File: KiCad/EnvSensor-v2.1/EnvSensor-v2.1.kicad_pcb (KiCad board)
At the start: 2 copper layers, 100 x 100 mm, 90 parts, among them J1 BattSense, J2 USB_B_Micro, J3 USB_C_Plug_USB2.0, J4 USB_C_Receptacle_USB2.0, J5 Conn_01x02, J6 Conn_01x02, Q1 AO6804A, Q2 IRLML2502, Q3 ZXMP6A16K, SW1 BATT_SWITCH, SW2 Start, U1 AP9101CK, U2 MCP1826S-5.0, U3 LM2735XMF, U4 MCP73843-4.2, U5 MCP1825S-3.3, U6 LTC3440

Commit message: pcb started
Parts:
- removed the J3 at (152.6, 105.2)
- added C13: 2u2, Capacitor_SMD:C_1206_3216Metric, F.Cu at (226.0, 162.0)
- added C14: 2u2, Capacitor_SMD:C_1206_3216Metric, F.Cu at (233.0, 163.0)
- added C16: 2u2, Capacitor_SMD:C_1206_3216Metric, F.Cu at (132.0, 144.0)
- added C17: 2u2, Capacitor_SMD:C_1206_3216Metric, F.Cu at (139.0, 144.0)
- added C19: 22u, Capacitor_SMD:C_1206_3216Metric, F.Cu at (133.0, 180.0)
- added C2: 4n7, Capacitor_SMD:C_0805_2012Metric, F.Cu at (193.2, 52.8)
- added C20: 22u, Capacitor_SMD:C_1206_3216Metric, F.Cu at (133.0, 186.0)
- added C21: 47u, Capacitor_SMD:C_1206_3216Metric, F.Cu at (162.0, 177.0)
- added C22: 47u, Capacitor_SMD:C_1206_3216Metric, F.Cu at (161.0, 182.0)
- added C26: 1u, Capacitor_SMD:C_0805_2012Metric, F.Cu at (66.0, 136.0)
- added C27: 47n, Capacitor_SMD:C_0805_2012Metric, F.Cu at (87.0, 165.0)
- added C33: 2u2, Capacitor_SMD:C_1206_3216Metric, F.Cu at (251.0, 94.0)
- added C35: 2u2, Capacitor_SMD:C_1206_3216Metric, F.Cu at (258.0, 94.0)
- added C36: 22n, Capacitor_SMD:C_0805_2012Metric, F.Cu at (83.0, 168.0)
- added C40: 2u2, Capacitor_SMD:C_1206_3216Metric, F.Cu at (191.0, 104.0)
- added C41: 2u2, Capacitor_SMD:C_1206_3216Metric, F.Cu at (197.0, 104.0)
- added C42: 100n, Capacitor_SMD:C_0603_1608Metric, F.Cu at (73.0, 169.0)
- added D1: PESD5V0V1BA, Diode_SMD:D_SOD-323, F.Cu at (108.0, 51.0)
- added D10: INPUT POWER LED, LED_THT:LED_D3.0mm_Horizontal_O3.81mm_Z6.0mm, F.Cu at (72.0, 141.0)
- added D11: POWER LED, LED_SMD:LED_0805_2012Metric, F.Cu at (83.0, 130.0)
- added D12: CHARGE LED, LED_THT:LED_D3.0mm_Horizontal_O3.81mm_Z6.0mm, F.Cu at (83.0, 135.0)
- added D13: 3.3V POWER LED, LED_THT:LED_D3.0mm_Horizontal_O3.81mm_Z6.0mm, F.Cu at (154.2, 49.8)
- added D14: 5V POWER LED, LED_THT:LED_D3.0mm_Horizontal_O3.81mm_Z6.0mm, F.Cu at (166.3, 49.8)
- added D9: POWER LED, LED_SMD:LED_0805_2012Metric, F.Cu at (73.0, 134.0)
- added J6: POWER_OUTPUT, Connector_PinHeader_2.54mm:PinHeader_2x07_P2.54mm_Vertical, F.Cu at (117.3, 90.6)
- added JP5: NC, Jumper:SolderJumper-2_P1.3mm_Bridged_RoundedPad1.0x1.5mm, F.Cu at (143.0, 172.0)
- added JP6: NO, Jumper:SolderJumper-2_P1.3mm_Open_RoundedPad1.0x1.5mm, F.Cu at (143.0, 176.0)
- added L2: 100-600, Inductor_SMD:L_0805_2012Metric, F.Cu at (228.0, 156.0)
- added L3: 100-600R, Inductor_SMD:L_0805_2012Metric, F.Cu at (137.0, 139.0)
- added L4: 1u, Inductor_SMD:L_TDK_SLF10145, F.Cu at (146.0, 192.0)
- added L6: 100-600R, Inductor_SMD:L_0805_2012Metric, F.Cu at (253.0, 89.0)
- added L7: 100-600R, Inductor_SMD:L_0805_2012Metric, F.Cu at (194.0, 101.0)
- added R16: 73k2, Resistor_SMD:R_0805_2012Metric, F.Cu at (155.0, 176.0)
- added R17: 120k, Resistor_SMD:R_0805_2012Metric, F.Cu at (155.0, 181.0)
- added R18: 3k3, Resistor_SMD:R_0805_2012Metric, F.Cu at (34.0, 141.0)
- added R2: 5k1, Resistor_SMD:R_0805_2012Metric, F.Cu at (108.0, 49.0)
- added R20: 30k, Resistor_SMD:R_0805_2012Metric, F.Cu at (155.0, 186.0)
- added R23: 4R7, Resistor_SMD:R_0805_2012Metric, F.Cu at (66.0, 130.0)
- added R24: DNP, Resistor_SMD:R_1206_3216Metric, F.Cu at (69.0, 158.0)
- added R25: 0R05, Resistor_SMD:R_1206_3216Metric, F.Cu at (69.0, 163.0)
- added R26: 10k, Resistor_SMD:R_0603_1608Metric, F.Cu at (78.0, 163.0)
- added R27: 3k3, Resistor_SMD:R_0805_2012Metric, F.Cu at (68.0, 145.0)
- added R28: 3k3, Resistor_SMD:R_0805_2012Metric, F.Cu at (85.0, 124.0)
- added R29: 3k3, Resistor_SMD:R_0805_2012Metric, F.Cu at (180.6, 67.4)
- added R30: 3k3, Resistor_SMD:R_0805_2012Metric, F.Cu at (176.1, 72.2)
- added R4: 50R, Resistor_SMD:R_2512_6332Metric, F.Cu at (161.8, 67.1)
- added R6: 12R5, Resistor_SMD:R_2512_6332Metric, F.Cu at (156.8, 62.2)
- added TP1: TestPoint, TestPoint:TestPoint_Pad_D1.5mm, F.Cu at (201.6, 53.3)
- added TP2: TestPoint, TestPoint:TestPoint_Pad_D1.5mm, F.Cu at (197.9, 56.0)
- added TP3: TestPoint, TestPoint:TestPoint_Pad_D1.5mm, F.Cu at (193.3, 62.6)
- added TP4: TestPoint, TestPoint:TestPoint_Pad_D1.5mm, F.Cu at (174.2, 80.3)
- added TP5: TestPoint, TestPoint:TestPoint_Pad_D1.5mm, F.Cu at (184.6, 70.7)
- added TP6: TestPoint, TestPoint:TestPoint_Pad_D1.5mm, F.Cu at (180.1, 73.6)
- added U4: TPS631000, Package_TO_SOT_SMD:SOT-23-8, F.Cu at (148.0, 179.0)
- added U7: LTC4052, Package_SO:MSOP-8_3x3mm_P0.65mm, F.Cu at (83.0, 155.0)
- C1: value 10n -> 4n7
- D2: renamed from D7; value PMEG2010AEJ -> DNP (PMEG2010AEJ)
- D3: renamed from D8; value PMEG3020BER -> DNP (PMEG3020BER)
- Q2: value IRLML2502 -> IRLML2244
- R1: value 3k -> 5k1
- R3: value 10k -> 100R; footprint Resistor_SMD:R_0603_1608Metric -> Resistor_SMD:R_2512_6332Metric
- R5: value 100k -> 25R; footprint Resistor_SMD:R_0603_1608Metric -> Resistor_SMD:R_2512_6332Metric
- TS1: renamed from TS4; footprint TestPoint:TestPoint_THTPad_D1.5mm_Drill0.7mm -> TestPoint:TestPoint_Pad_D1.5mm
- TS2: renamed from TS5; footprint TestPoint:TestPoint_THTPad_D1.5mm_Drill0.7mm -> TestPoint:TestPoint_Pad_D1.5mm
- TS3: renamed from TS6; footprint TestPoint:TestPoint_THTPad_D1.5mm_Drill0.7mm -> TestPoint:TestPoint_Pad_D1.5mm
- TS4: renamed from TS7; footprint TestPoint:TestPoint_THTPad_D1.5mm_Drill0.7mm -> TestPoint:TestPoint_Pad_D1.5mm
- TS5: renamed from TS1; footprint TestPoint:TestPoint_THTPad_D1.5mm_Drill0.7mm -> TestPoint:TestPoint_Pad_D1.5mm
- TS6: renamed from TS2; footprint TestPoint:TestPoint_THTPad_D1.5mm_Drill0.7mm -> TestPoint:TestPoint_Pad_D1.5mm
- TS7: renamed from TS3; footprint TestPoint:TestPoint_THTPad_D1.5mm_Drill0.7mm -> TestPoint:TestPoint_Pad_D1.5mm
- moved D7 259.7 mm to (40.0, 157.0)
- moved R21 258.4 mm to (33.0, 163.0)
- moved C23 235.1 mm to (49.0, 135.0)
- moved D5 234.3 mm to (23.0, 138.0)
- moved H1 217.8 mm to (26.0, 24.0)
- moved D6 214.9 mm to (22.0, 131.0)
- moved C24 208.9 mm to (49.0, 154.0)
- moved C18 208.6 mm to (30.0, 136.0)
- moved H4 204.3 mm to (23.0, 116.0)
- moved Q2 203.9 mm to (34.0, 132.0)
- moved C25 186.7 mm to (50.0, 161.0)
- moved R19 174.7 mm to (23.0, 145.0)
- moved R1 156.3 mm to (108.0, 47.0), turned to 180 degrees
- moved U5 132.0 mm to (26.0, 156.0)
- moved R22 128.6 mm to (33.0, 148.0)
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- renumbered C23 to C10, C24 to C11, C25 to C12, C20 to C15, C3 to C18, C4 to C23, C14 to C24, C15 to C25, C5 to C28, C6 to C29, C16 to C3, C7 to C30, C8 to C31, C9 to C32, C10 to C34, C11 to C37, C12 to C38, C13 to C39, C17 to C4, C18 to C5, C19 to C6, C2 to C7, C21 to C8, C22 to C9, D2 to D15, D1 to D4, D3 to D5, D4 to D6, D5 to D7, D6 to D8, J2 to J1, J4 to J2, J1 to J3, J6 to J4, JP4 to JP2, JP5 to JP3, JP3 to JP4, JP2 to JP7, L2 to L1, L1 to L5, R15 to R10, R16 to R11, R17 to R12, R18 to R13, R19 to R14, R6 to R15, R8 to R19, R11 to R21, R12 to R22, R7 to R31, R9 to R32, R10 to R33, R13 to R34, R2 to R7, R14 to R8, R4 to R9, U6 to U1, U1 to U2, U5 to U3, U4 to U5, U2 to U6, U3 to U8
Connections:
- net Net-(C20-Pad1) renamed /3V3_REG
- net Net-(D8-Pad2) renamed /3V3_LTC_SW2
- net Net-(R14-Pad2) renamed /3V3_LTC_FB
- C1 pad 1: BATTERY_MEASURE_INPUT -> Net-(C1-Pad1)
- C10 pad 1: +BATT -> /BATT_3V3_FILTER
- C18 pad 1: Net-(C3-Pad1) -> Net-(C18-Pad1)
- C28 pad 1: Net-(C5-Pad1) -> Net-(C28-Pad1)
- C29 pad 1: Net-(C5-Pad1) -> Net-(C28-Pad1)
- C3 pad 1: Net-(C16-Pad1) -> /3V3_NOT_REG
- C30 pad 1: Net-(C5-Pad1) -> Net-(C28-Pad1)
- C31 pad 1: Net-(C5-Pad1) -> Net-(C28-Pad1)
- C32 pad 1: Net-(C5-Pad1) -> Net-(C28-Pad1)
- C37 pad 1: +BATT -> Net-(C37-Pad1)
- C38 pad 1: +BATT -> Net-(C37-Pad1)
- C39 pad 1: +BATT -> Net-(C37-Pad1)
- C4 pad 1: Net-(C16-Pad1) -> /3V3_NOT_REG
- C5 pad 1: Net-(C16-Pad1) -> /3V3_NOT_REG
- C6 pad 1: Net-(C16-Pad1) -> /3V3_NOT_REG
- C8 pad 1: +BATT -> /BATT_3V3_FILTER
- C9 pad 1: +BATT -> /BATT_3V3_FILTER
- D15 pad 1: Net-(C5-Pad1) -> Net-(C28-Pad1)
- D2 pad 1: Net-(D7-Pad1) (its old number) -> /3V3_LTC_SW1
- D3 pad 1: Net-(C16-Pad1) -> /3V3_NOT_REG
- D4 pad 1: Net-(C3-Pad1) -> unconnected-(D4-Pad1)
- D4 pad 2: VBUS -> unconnected-(D4-Pad2)
- D7 pad 2: Net-(C3-Pad1) -> Net-(C18-Pad1)
- D8 pad 2: Net-(C3-Pad1) -> Net-(C18-Pad1)
- J1 pad 6: unconnected-(J2-Pad6) -> Net-(C1-Pad1)
- J2 pad A1: Net-(J4-PadA1) -> GND
- J2 pad A12: Net-(J4-PadA1) -> GND
- J2 pad A4: Net-(J4-PadA4) -> VBUS
- J2 pad A5: unconnected-(J4-PadA5) -> Net-(J2-PadA5)
- J2 pad A9: Net-(J4-PadA4) -> VBUS
- J2 pad B1: Net-(J4-PadA1) -> GND
- J2 pad B12: Net-(J4-PadA1) -> GND
- J2 pad B4: Net-(J4-PadA4) -> VBUS
- J2 pad B5: unconnected-(J4-PadB5) -> Net-(J2-PadB5)
- J2 pad B9: Net-(J4-PadA4) -> VBUS
- J2 pad S1: unconnected-(J4-PadS1) -> Net-(C2-Pad1)
- JP2 pad 1: +BATT -> /BATT_3V3_FILTER
- L1 pad 1: Net-(D7-Pad1) (its old number) -> /3V3_LTC_SW1
- L5 pad 1: +BATT -> Net-(C37-Pad1)
- Q2 pad 1: BATTERY_MEASURE_ENABLE -> Net-(Q2-Pad1)
- Q2 pad 2: GND -> Net-(C18-Pad1)
- Q2 pad 3: Net-(Q2-Pad3) -> VBUS
- R1 pad 1: +BATT -> Net-(J2-PadB5)
- R1 pad 2: BATTERY_MEASURE_INPUT -> GND
- R15 pad 2: Net-(C3-Pad1) -> Net-(C18-Pad1)
- R22 pad 2: Net-(C3-Pad1) -> Net-(C18-Pad1)
- R3 pad 1: BATTERY_MEASURE_INPUT -> Net-(R3-Pad1)
- R3 pad 2: Net-(Q2-Pad3) -> GND
- R31 pad 1: Net-(C5-Pad1) -> Net-(C28-Pad1)
- R5 pad 1: BATTERY_MEASURE_ENABLE -> Net-(R5-Pad1)
- R8 pad 1: Net-(C16-Pad1) -> /3V3_NOT_REG
- TS1 pad 1: Net-(D7-Pad1) (its old number) -> /3V3_LTC_SW1
- TS3 pad 1: Net-(C16-Pad1) -> /3V3_NOT_REG
- TS4 pad 1: +BATT -> /BATT_3V3_FILTER
- TS6 pad 1: Net-(C5-Pad1) -> Net-(C28-Pad1)
- TS7 pad 1: +BATT -> Net-(C37-Pad1)
- U1 pad 3: Net-(D7-Pad1) (its old number) -> /3V3_LTC_SW1
- U1 pad 6: Net-(C16-Pad1) -> /3V3_NOT_REG
- U1 pad 7: +BATT -> /BATT_3V3_FILTER
- U1 pad 8: +BATT -> /BATT_3V3_FILTER
- U3 pad 1: Net-(C16-Pad1) -> Net-(C14-Pad1)
- U5 pad 2: Net-(C3-Pad1) -> Net-(C18-Pad1)
- U6 pad 1: Net-(C5-Pad1) -> Net-(C35-Pad1)
- U8 pad 5: +BATT -> Net-(C37-Pad1)

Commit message: More pcb work
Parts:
- removed C2: 4n7, Capacitor_SMD:C_0805_2012Metric
- removed D10: INPUT POWER LED, LED_THT:LED_D3.0mm_Horizontal_O3.81mm_Z6.0mm
- removed D11, D9: POWER LED, LED_SMD:LED_0805_2012Metric
- removed D12: CHARGE LED, LED_THT:LED_D3.0mm_Horizontal_O3.81mm_Z6.0mm
- removed D8: CHARGE LED - Red, LED_THT:LED_D3.0mm_Horizontal_O3.81mm_Z6.0mm
- removed R27, R28: 3k3, Resistor_SMD:R_0805_2012Metric
- added C43: 100n, Capacitor_SMD:C_0603_1608Metric, B.Cu at (95.0, 50.0)
- added F1: 0ZCJ0110FF2E, Fuse:Fuse_1206_3216Metric, F.Cu at (46.0, 113.5)
- added F2: 0ZCJ0110FF2E, Fuse:Fuse_1206_3216Metric, F.Cu at (70.0, 113.5)
- added F3: 0ZCJ0110FF2E, Fuse:Fuse_1206_3216Metric, F.Cu at (94.0, 113.5)
- added JP8: NO, Jumper:SolderJumper-2_P1.3mm_Open_RoundedPad1.0x1.5mm, B.Cu at (115.2, 61.8)
- added JP9: NO, Jumper:SolderJumper-2_P1.3mm_Open_RoundedPad1.0x1.5mm, B.Cu at (112.8, 61.8)
- C10, C11, C12, C15, C18, C19, C20, C21, C22, C23, C24, C25, C26, C27, C28, C29, C3, C30, C31, C32, C34, C36, C37, C38, C39, C4, C42, C5, C6, C8, C9, D15, D2, D3, J4, J5, JP2, JP3, JP4, JP5, JP6, JP7, L1, L2, L3, L4, L5, L6, L7, Q2, Q3, R10, R11, R12, R13, R14, R15, R16, R17, R18, R19, R20, R21, R22, R23, R24, R25, R26, R29, R3, R30, R31, R32, R33, R34, R4, R5, R6, R8, TP1, TP2, TP3, TP4, TP5, TP6, TS1, TS2, TS3, TS4, TS5, TS6, TS7, U1, U3, U5, U6, U7, U8: moved to B.Cu
- C13, C14, C16, C17, C33, C35, C40, C41: footprint Capacitor_SMD:C_1206_3216Metric -> Capacitor_SMD:C_0805_2012Metric; moved to B.Cu
- D13, D14: footprint LED_THT:LED_D3.0mm_Horizontal_O3.81mm_Z6.0mm -> LED_SMD:LED_0805_2012Metric; moved to B.Cu
- D4: value PMEG3020BER -> POWER LED; footprint Diode_SMD:D_SOD-123 -> LED_SMD:LED_0805_2012Metric
- D6: value POWER LED -> POWER LED (Red)
- D7: value CHARGE LED - Red -> CHARGE LED (Red); footprint LED_SMD:LED_0805_2012Metric -> LED_THT:LED_D3.0mm_Horizontal_O3.81mm_Z6.0mm
- U4: footprint Package_TO_SOT_SMD:SOT-23-8 -> JPPackages:SOT-5x3; moved to B.Cu
- moved JP7 238.0 mm to (45.0, 92.0), turned to 180 degrees
- moved J5 236.9 mm to (46.3, 89.0), turned to 90 degrees
- moved U6 230.3 mm to (40.8, 83.2), turned to 180 degrees
- moved C34 225.9 mm to (46.5, 84.8), turned to 90 degrees
- moved C35 217.6 mm to (41.0, 78.2), turned to 180 degrees
- moved L6 211.4 mm to (42.0, 75.5), turned to -90 degrees
- moved C33 211.1 mm to (41.0, 72.8), turned to 180 degrees
- moved J4 209.7 mm to (55.2, 92.2), turned to 180 degrees
- moved JP4 207.8 mm to (56.2, 100.2), turned to 180 degrees
- moved C31 205.4 mm to (41.0, 67.8), turned to 180 degrees
- moved C29 205.3 mm to (41.0, 63.2), turned to 180 degrees
- moved C30 203.9 mm to (41.0, 65.5), turned to 180 degrees
- moved C32 202.1 mm to (41.0, 70.0), turned to 180 degrees
- moved C28 201.6 mm to (36.0, 69.0)
- moved TS6 200.5 mm to (33.2, 68.0), turned to -90 degrees
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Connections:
- net Net-(C11-Pad2) renamed /3V3_LTC_VC
- net Net-(C14-Pad1) renamed /3V3_FILTER
- net Net-(C24-Pad1) renamed /L_CHRG_TIMER
- net Net-(C27-Pad2) renamed /I_CHRG_GATE
- net Net-(C28-Pad1) renamed /5V_NOT_REG
- net Net-(C28-Pad2) renamed /5V_FB
- net Net-(C35-Pad1) renamed /5V_FILTERED
- net Net-(C37-Pad1) renamed /5V_IN
- net Net-(C42-Pad1) renamed /I_CHRG_TIMER
- net Net-(C7-Pad1) renamed /PROT_VDD
- net Net-(JP2-Pad2) renamed /3V3_LTC_MODE
- net Net-(JP5-Pad2) renamed /3V3_TSP_MODE
- net Net-(L4-Pad1) renamed /3V3_TSP_LX1
- net Net-(L4-Pad2) renamed /3V3_TSP_LX2
- net Net-(Q1-Pad2) renamed /PROT_DRAIN
- net Net-(Q3-Pad1) renamed /L_CHRG_DRV
- net Net-(Q3-Pad3) renamed /L_CHRG_SENSE
- net Net-(R12-Pad1) renamed /3V3_LTC_Rt
- net Net-(R17-Pad1) renamed /3V3_TSP_FB
- net Net-(R22-Pad1) renamed /L_CHRG_EN
- net Net-(R24-Pad2) renamed /I_CHRG_SENSE
- B1 pad 2: -BATT -> /BATT1-
- B2 pad 2: -BATT -> /BATT2-
- B3 pad 2: -BATT -> /BATT3-
- C1 pad 1: Net-(C1-Pad1) -> /USB_SHIELD
- C18 pad 1: Net-(C18-Pad1) -> /L_CHRG_POWER
- D4 pad 1: unconnected-(D4-Pad1) -> Net-(D4-Pad1)
- D4 pad 2: unconnected-(D4-Pad2) -> VBUS
- D7 pad 1: Net-(D7-Pad1) -> Net-(D4-Pad1)
- D7 pad 2: Net-(C18-Pad1) -> VBUS
- J1 pad 6: Net-(C1-Pad1) -> /USB_SHIELD
- J2 pad S1: Net-(C2-Pad1) -> /USB_SHIELD
- J3 pad 1: Net-(J3-Pad1) -> /BATT_SW
- JP1 pad 1: Net-(J3-Pad1) -> /BATT_SW
- Q2 pad 2: Net-(C18-Pad1) -> /L_CHRG_POWER
- R15 pad 2: Net-(C18-Pad1) -> /L_CHRG_POWER
- R19 pad 1: GND -> Net-(R19-Pad1)
- R21 pad 1: Net-(D7-Pad1) -> /CHRG_CHRG
- R21 pad 2: Net-(R21-Pad2) -> Net-(D4-Pad1)
- R22 pad 2: Net-(C18-Pad1) -> /L_CHRG_POWER
- R7 pad 1: Net-(J3-Pad1) -> +BATT
- SW1 pad 2: Net-(J3-Pad1) -> /BATT_SW
- U5 pad 2: Net-(C18-Pad1) -> /L_CHRG_POWER
- U5 pad 3: Net-(R21-Pad2) -> /CHRG_CHRG
- U7 pad 2: Net-(R27-Pad1) -> /CHRG_ACPR
- U7 pad 6: Net-(R28-Pad1) -> /CHRG_CHRG
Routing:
- net VBUS: track 0.00 -> 134.7 mm, vias 0 -> 2
- net +BATT: track 0.00 -> 84.2 mm
- net -BATT: track 0.00 -> 77.5 mm
- net /CHRG_CHRG: track 0.00 -> 69.4 mm, vias 0 -> 2
- net /BATT_BARE: track 0.00 -> 59.4 mm
- net GND: track 0.00 -> 40.2 mm, vias 0 -> 20
- net /CHRG_ACPR: track 0.00 -> 25.8 mm
- net /BATT_SW: track 0.00 -> 19.5 mm
- net /L_CHRG_POWER: track 0.00 -> 9.98 mm
- net Net-(Q1-Pad4): track 0.00 -> 8.65 mm, vias 0 -> 2
- net /L_CHRG_SENSE: track 0.00 -> 8.63 mm
- net /L_CHRG_DRV: track 0.00 -> 8.32 mm
- net /BATT3-: track 0.00 -> 8.23 mm
- net /BATT2-: track 0.00 -> 8.23 mm
- net /BATT1-: track 0.00 -> 8.23 mm
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- added copper zone on B.Cu, net /I_CHRG_SENSE
- added copper zone on F.Cu, net /USB_SHIELD
- added copper zone on In1.Cu, net GND
- added copper zone on In2.Cu, net GND
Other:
- copper layers 2 -> 4
- board text added: "Charging"
- board text added: "Power"
- board text added: "Start"

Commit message: more work
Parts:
- removed C32: 22u, Capacitor_SMD:C_1206_3216Metric
- removed C39: 10u, Capacitor_SMD:C_0805_2012Metric
- added C2: 10u, Capacitor_SMD:C_1206_3216Metric, B.Cu at (43.8, 67.8)
- added U2: E-Ink_Waveshare_4.2, JPDisplays:4.2inch_E-Ink, F.Cu at (20.0, 200.0)
- C29, C30: value 22u -> 10u
- moved J3 25.4 mm to (70.5, 24.5)
- moved JP1 25.4 mm to (71.7, 27.2)
- moved SW1 23.0 mm to (52.5, 23.1)
- moved J5 22.2 mm to (27.0, 100.0), turned to 0 degrees
- moved C31 21.7 mm to (48.5, 88.1), turned to 90 degrees
- moved C6 17.2 mm to (66.8, 95.3), turned to 90 degrees
- moved JP7 16.4 mm to (30.0, 98.8), turned to 90 degrees
- moved J4 12.7 mm to (52.0, 104.5), turned to 0 degrees
- moved TP2 12.6 mm to (26.8, 64.2)
- moved C28 9.42 mm to (40.0, 60.5)
- moved R31 9.42 mm to (40.0, 58.5)
- moved R33 9.42 mm to (40.0, 56.5)
- moved R34 9.42 mm to (40.0, 54.5)
- moved C15 8.69 mm to (57.2, 95.3), turned to 90 degrees
- moved C34 8.24 mm to (39.0, 88.1)
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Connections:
- net Net-(C34-Pad1) renamed /5V_REG
- C31 pad 1: /5V_NOT_REG -> /5V_FILTERED
- C6 pad 1: /3V3_NOT_REG -> /3V3_FILTER
- J6 pad 1: VBUS -> +5V
- J6 pad 11: +BATT -> VBUS
- J6 pad 5: +5V -> +3V3
- J6 pad 9: +3V3 -> +BATT
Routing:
- net GND: track 40.2 -> 147.0 mm, vias 20 -> 63
- net /3V3_NOT_REG: track 0.00 -> 73.7 mm, vias 0 -> 2
- net +BATT: track 84.2 -> 151.6 mm, vias 0 -> 5
- net +3V3: track 0.00 -> 43.5 mm
- net /BATT_3V3_FILTER: track 0.00 -> 27.7 mm
- net /5V_NOT_REG: track 0.00 -> 26.8 mm
- net /CHRG_CHRG: track 69.4 -> 46.5 mm, vias 2 -> 1
- net /5V_REG: track 0.00 -> 21.1 mm
- net /5V_FILTERED: track 0.00 -> 20.4 mm
- net +5V: track 0.00 -> 17.5 mm
- net /3V3_FILTER: track 0.00 -> 14.6 mm
- net /3V3_REG: track 0.00 -> 14.5 mm
- net /5V_IN: track 0.00 -> 13.4 mm
- net /3V3_LTC_SW1: track 0.00 -> 13.4 mm
- net /3V3_LTC_SW2: track 0.00 -> 13.0 mm
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- added copper zone on B.Cu, net +BATT
- added copper zone on B.Cu, net /3V3_NOT_REG
- added copper zone on B.Cu, net /5V_IN
- added copper zone on B.Cu, net /5V_NOT_REG
- added copper zone on B.Cu, net /5V_SW
- added copper zone on B.Cu, net /BATT_3V3_FILTER

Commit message: pcb
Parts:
- removed the U2 at (20.0, 200.0)
- C1, D1, J1, J2, R1, R2: moved to B.Cu
- moved D13 106.2 mm to (135.0, 96.1), turned to 90 degrees
- moved D14 105.2 mm to (135.0, 91.8), turned to -90 degrees
- moved R29 102.2 mm to (133.0, 96.1), turned to -90 degrees
- moved R30 101.3 mm to (133.0, 91.8), turned to 90 degrees
- moved D7 96.3 mm to (22.6, 61.5), turned to -90 degrees
- moved D6 95.3 mm to (22.6, 71.5), turned to -90 degrees
- moved J1 94.5 mm to (22.5, 37.4)
- moved J2 94.0 mm to (23.0, 51.8)
- moved J6 92.1 mm to (116.2, 76.6), turned to 0 degrees
- moved JP8 91.3 mm to (25.1, 76.2), turned to -90 degrees
- moved D4 91.0 mm to (25.1, 62.8), turned to -90 degrees
- moved R21 91.0 mm to (25.1, 62.8), turned to 90 degrees
- moved D5 90.5 mm to (25.1, 72.8), turned to -90 degrees
- moved R19 90.5 mm to (25.1, 72.8), turned to 90 degrees
- moved C1 89.5 mm to (25.0, 45.5), turned to 0 degrees
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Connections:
- J6 pad 1: +5V -> +3V3
- J6 pad 3: +5V -> +3V3
- J6 pad 5: +3V3 -> +5V
- J6 pad 7: +3V3 -> +5V
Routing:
- net +BATT: track 151.6 -> 34.4 mm, vias 5 -> 1
- net VBUS: track 135.2 -> 73.5 mm, vias 2 -> 1
- net +3V3: track 43.5 -> 3.02 mm
- net /CHRG_CHRG: track 46.5 -> 14.7 mm
- net /CHRG_ACPR: track 25.8 -> 3.63 mm
- net /5V_REG: track 21.1 -> 3.26 mm
- net -BATT: track 77.7 -> 62.5 mm, vias 0 -> 1
- net +5V: track 17.5 -> 3.25 mm
- net /5V_FILTERED: track 20.4 -> 7.16 mm
- net /BATT_3V3_FILTER: track 27.7 -> 14.6 mm
- net /3V3_REG: track 14.5 -> 4.57 mm
- net /5V_IN: track 13.4 -> 3.82 mm
- net /BATT_BARE: track 59.0 -> 67.5 mm
- net /BATT2-: track 8.23 -> 0.00 mm
- net /3V3_FILTER: track 14.6 -> 6.49 mm
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- added copper zone on B.Cu, net /USB_SHIELD
- removed copper zone on F.Cu, net /USB_SHIELD
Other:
- board size 100 x 100 mm -> 102 x 100 mm
- board text added: "3V3 Buck-Bust Converter (LTC3440 or TPS631000)"
- board text added: "5V Bust Converter (LM2735XMF)"
- board text added: "Impulse Charger (LTC4052)"
- board text added: "Linear Charger (MCP73843-4.2)"
- board text added: "aabb"

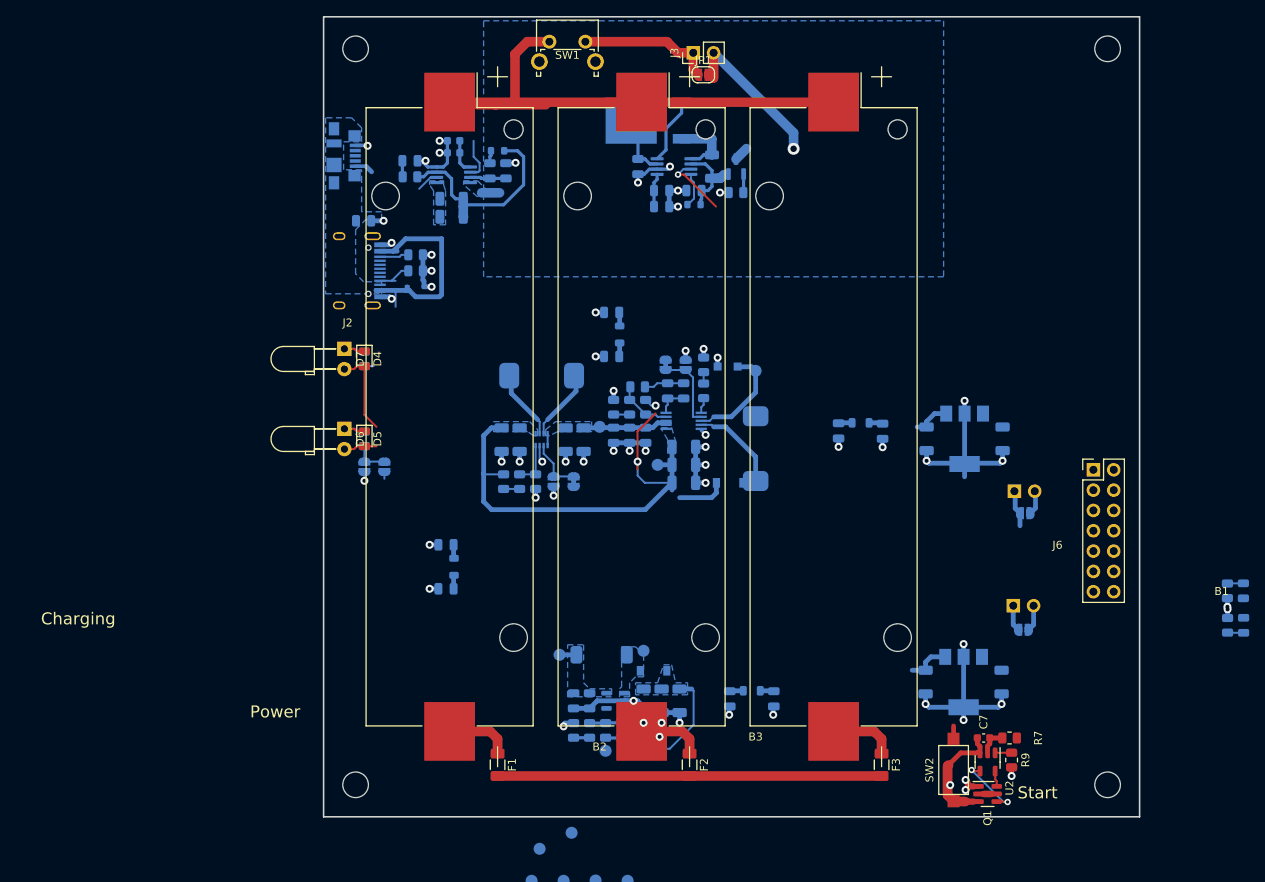
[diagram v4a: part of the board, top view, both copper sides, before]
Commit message: Upgrade to STM32CubeIDE 1.12
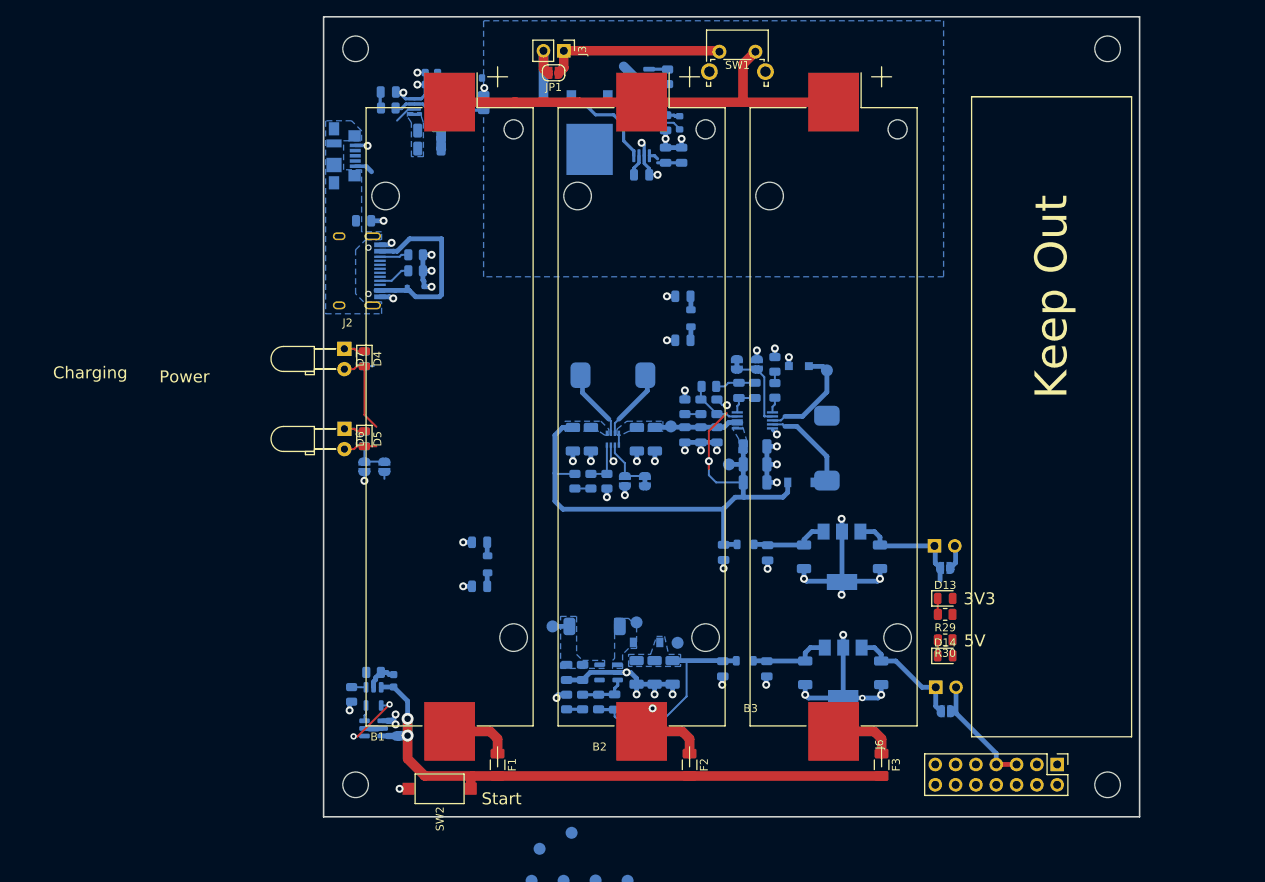
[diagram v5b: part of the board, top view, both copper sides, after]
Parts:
- C7, Q1, R7, R9, U2: moved to B.Cu
- D13, D14, R29, R30: moved to F.Cu
- moved R9 82.9 mm to (23.5, 104.7)
- moved R7 79.9 mm to (26.2, 102.0), turned to 0 degrees
- moved Q1 77.2 mm to (26.2, 109.0), turned to 180 degrees
- moved U2 77.2 mm to (26.2, 105.0)
- moved C7 74.1 mm to (28.8, 103.0), turned to -90 degrees
- moved SW2 64.3 mm to (34.5, 116.5), turned to 180 degrees
- moved D14 38.2 mm to (97.7, 99.9), turned to 0 degrees
- moved D13 37.5 mm to (97.7, 92.7), turned to 0 degrees
- moved J6 37.1 mm to (111.7, 113.5), turned to -90 degrees
- moved R30 35.8 mm to (97.7, 97.9), turned to 180 degrees
- moved R29 35.3 mm to (97.7, 94.7), turned to 180 degrees
- moved SW1 21.3 mm to (69.5, 24.4)
- moved C15 21.3 mm to (89.5, 87.5)
- moved C6 21.3 mm to (80.0, 87.5)
- moved U3 21.3 mm to (84.8, 87.5)
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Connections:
- SW1 pad 1: /BATT_BARE -> /BATT_SW
- SW1 pad 2: /BATT_SW -> /BATT_BARE
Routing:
- net +BATT: track 34.4 -> 15.0 mm, vias 1 -> 0
- net VBUS: track 73.5 -> 54.9 mm, vias 1 -> 0
- net -BATT: track 62.5 -> 78.3 mm, vias 1 -> 2
- net /CHRG_CHRG: track 14.7 -> 1.16 mm, vias 1 -> 0
- net GND: track 153.7 -> 140.7 mm, vias 60 -> 59
- net /BATT_BARE: track 67.5 -> 55.0 mm
- net /5V_REG: track 3.26 -> 15.1 mm
- net +5V: track 3.25 -> 14.3 mm
- net /3V3_REG: track 4.57 -> 15.1 mm
- net /BATT2-: track 0.00 -> 9.32 mm, vias 0 -> 1
- net /L_CHRG_SENSE: track 8.63 -> 2.84 mm
- net /3V3_NOT_REG: track 69.7 -> 75.4 mm
- net /BATT_SW: track 17.1 -> 22.5 mm
- net /5V_NOT_REG: track 21.1 -> 25.6 mm
- net /L_CHRG_DRV: track 8.32 -> 12.3 mm
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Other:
- board text added: "3V3"
- board text added: "5V"
- board text added: "Batt prot (AP9101CK)"
- board text added: "Keep Out"
